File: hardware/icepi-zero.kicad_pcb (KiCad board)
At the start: 4 copper layers, 65 x 30 mm, 133 parts, among them J1 Conn_02x20_Counter_Clockwise, J2 HDMI_C_1.3, J3 USB_C_Receptacle_USB2.0_14P, J4 USB_C_Receptacle_USB2.0_14P, J5 USB_C_Receptacle_USB2.0_14P, J6 Micro_SD_Card_Det2, U1 TLV62569DBV, U10 W9825G6KH, U11 W25Q128JVS, U2 TLV62569DBV, U3 ECP5U_12_CABGA256, U4 TLV62569DBV, U5 PCA9306DC1, U6 FT231XQ, U7 TPD2EUSB30A, U8 TPD2EUSB30A, U9 TPD2EUSB30A, Y1 SIT8008xx-1x-xxE-100.000000

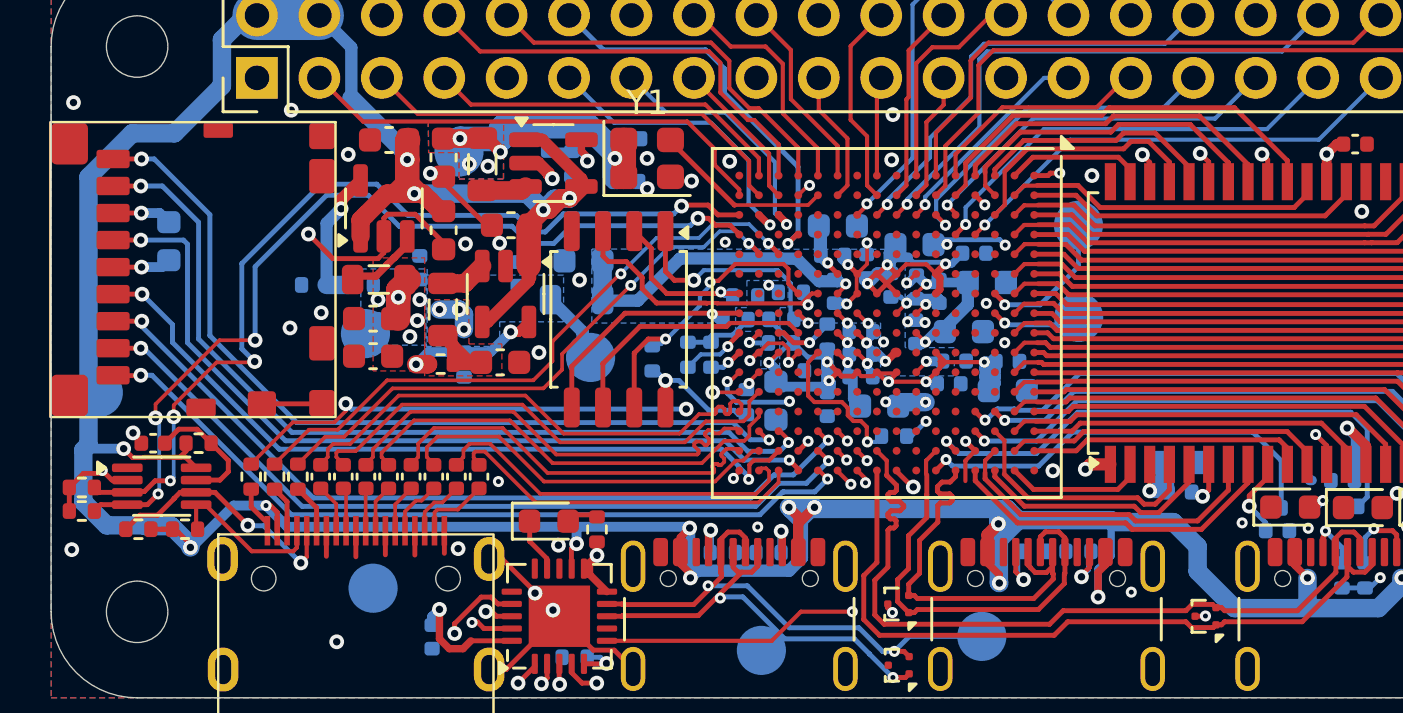
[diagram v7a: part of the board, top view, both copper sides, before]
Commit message: Add a button
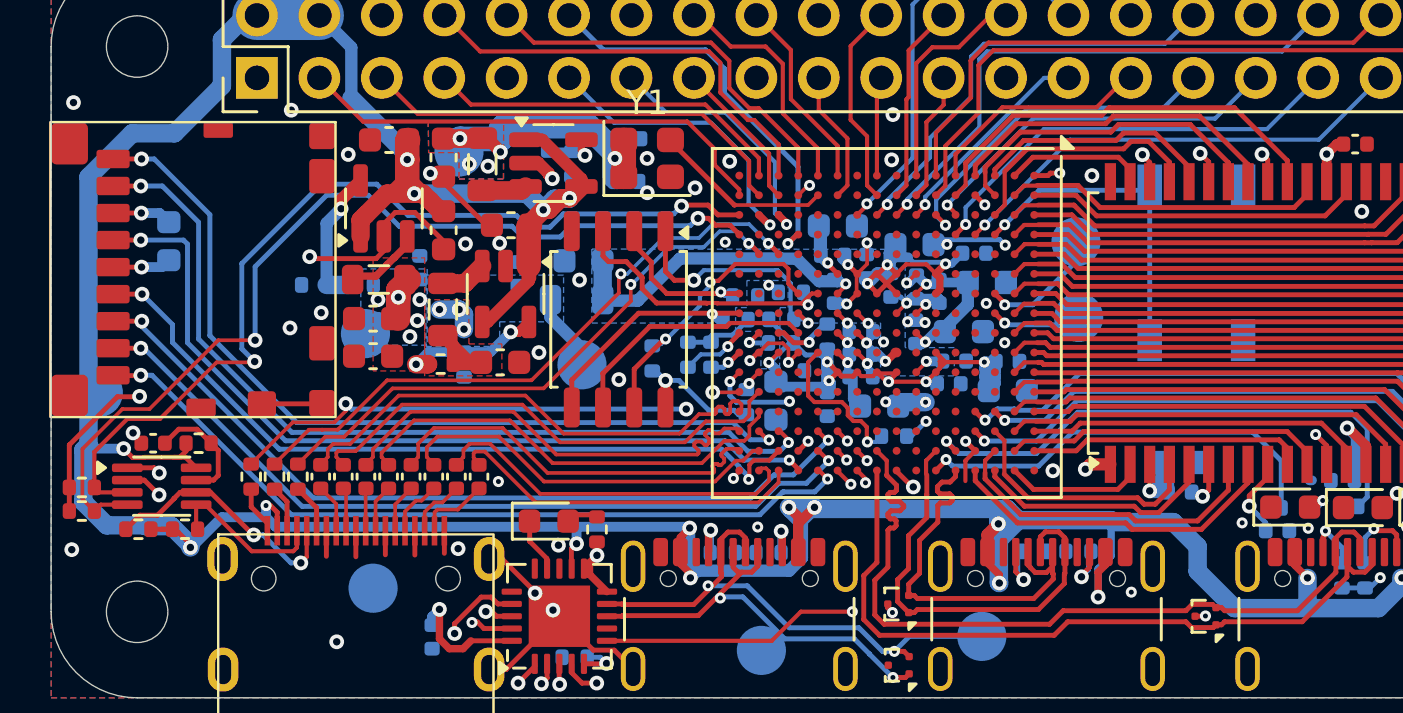
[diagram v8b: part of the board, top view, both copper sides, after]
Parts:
- added SW1: SW_Push, Button_Switch_SMD:SW_SPST_TL3342, B.Cu at (162.6, 102.3)
- moved TP9 0.68 mm to (157.7, 101.5)
- moved TP6 0.46 mm to (137.6, 106.5)
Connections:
- U3 pad C4: unconnected-(U3B-PT11A/+-PadC4) -> SW1
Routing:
- net SW1: track 0.00 -> 13.4 mm, vias 0 -> 1
- net +3V3: track 92.6 -> 96.7 mm, vias 27 -> 28
- net FPDI_SDA: track 37.2 -> 38.2 mm, vias 4 -> 2
- net GND: track 76.7 -> 77.6 mm, vias 78 -> 80
- net Net-(U4-FB): track 2.75 -> 2.24 mm
- net FPDI_SCL: track 37.7 -> 38.0 mm, vias 4 -> 2
